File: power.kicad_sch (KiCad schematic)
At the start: 44 parts, among them IC302 L7805, IC303 L7805, J101 Test Points, P302 POWER, Q106 15 29, Q308 FR 32, Q503 BR 29, SW101 SW_SPDT

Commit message: General clean-up.
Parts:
- added TP2: ~, A-PCENGINE:Test_Point_1.5mm, symbol Connector:TestPoint
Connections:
- net +9V: now also TP2.1
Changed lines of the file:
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@@
   (junction (at 270.51 106.68) (diameter 0) (color 0 0 0 0)
+  )
+  (junction (at 253.365 36.83) (diameter 0) (color 0 0 0 0)
   )
   (junction (at 285.75 151.13) (diameter 0) (color 0 0 0 0)
@@
   )
   (wire (pts (xy 147.32 156.21) (xy 147.32 158.75))
+    (stroke (width 0) (type default))
+  )
+  (wire (pts (xy 253.365 36.83) (xy 256.286 36.83))
     (stroke (width 0) (type default))
   )
@@
         )
       )
+    )
+  )
+  (symbol (lib_id "Connector:TestPoint") (at 256.286 36.83 0) (unit 1)
+    (in_bom yes) (on_board yes) (dnp no)
+    (property "Reference" "TP2" (at 256.286 27.305 90)
+      (effects (font (size 1.27 1.27)) (justify right))
+    )
+    (property "Value" "~" (at 254.381 32.258 0)
+      (effects (font (size 1.27 1.27)) (justify right))
+    )
+    (property "Footprint" "A-PCENGINE:Test_Point_1.5mm" (at 261.366 36.83 0)
+      (effects (font (size 1.27 1.27)) hide)
+    )
+    (property "Datasheet" "~" (at 261.366 36.83 0)
+      (effects (font (size 1.27 1.27)) hide)
+    )
+    (pin "1")
+    (instances
+      (project "PCE"
+        (path "/c1c718c6-a427-431e-a18b-e46f94ae8e09/bb2f9872-1813-43e0-bcfc-5c5426bf43ce"
+          (reference "TP2") (unit 1)
+        )
+        (path "/c1c718c6-a427-431e-a18b-e46f94ae8e09/ba362b1f-3cb7-4861-9385-2b05dca17551"
+          (reference "TP70") (unit 1)
+        )
+      )

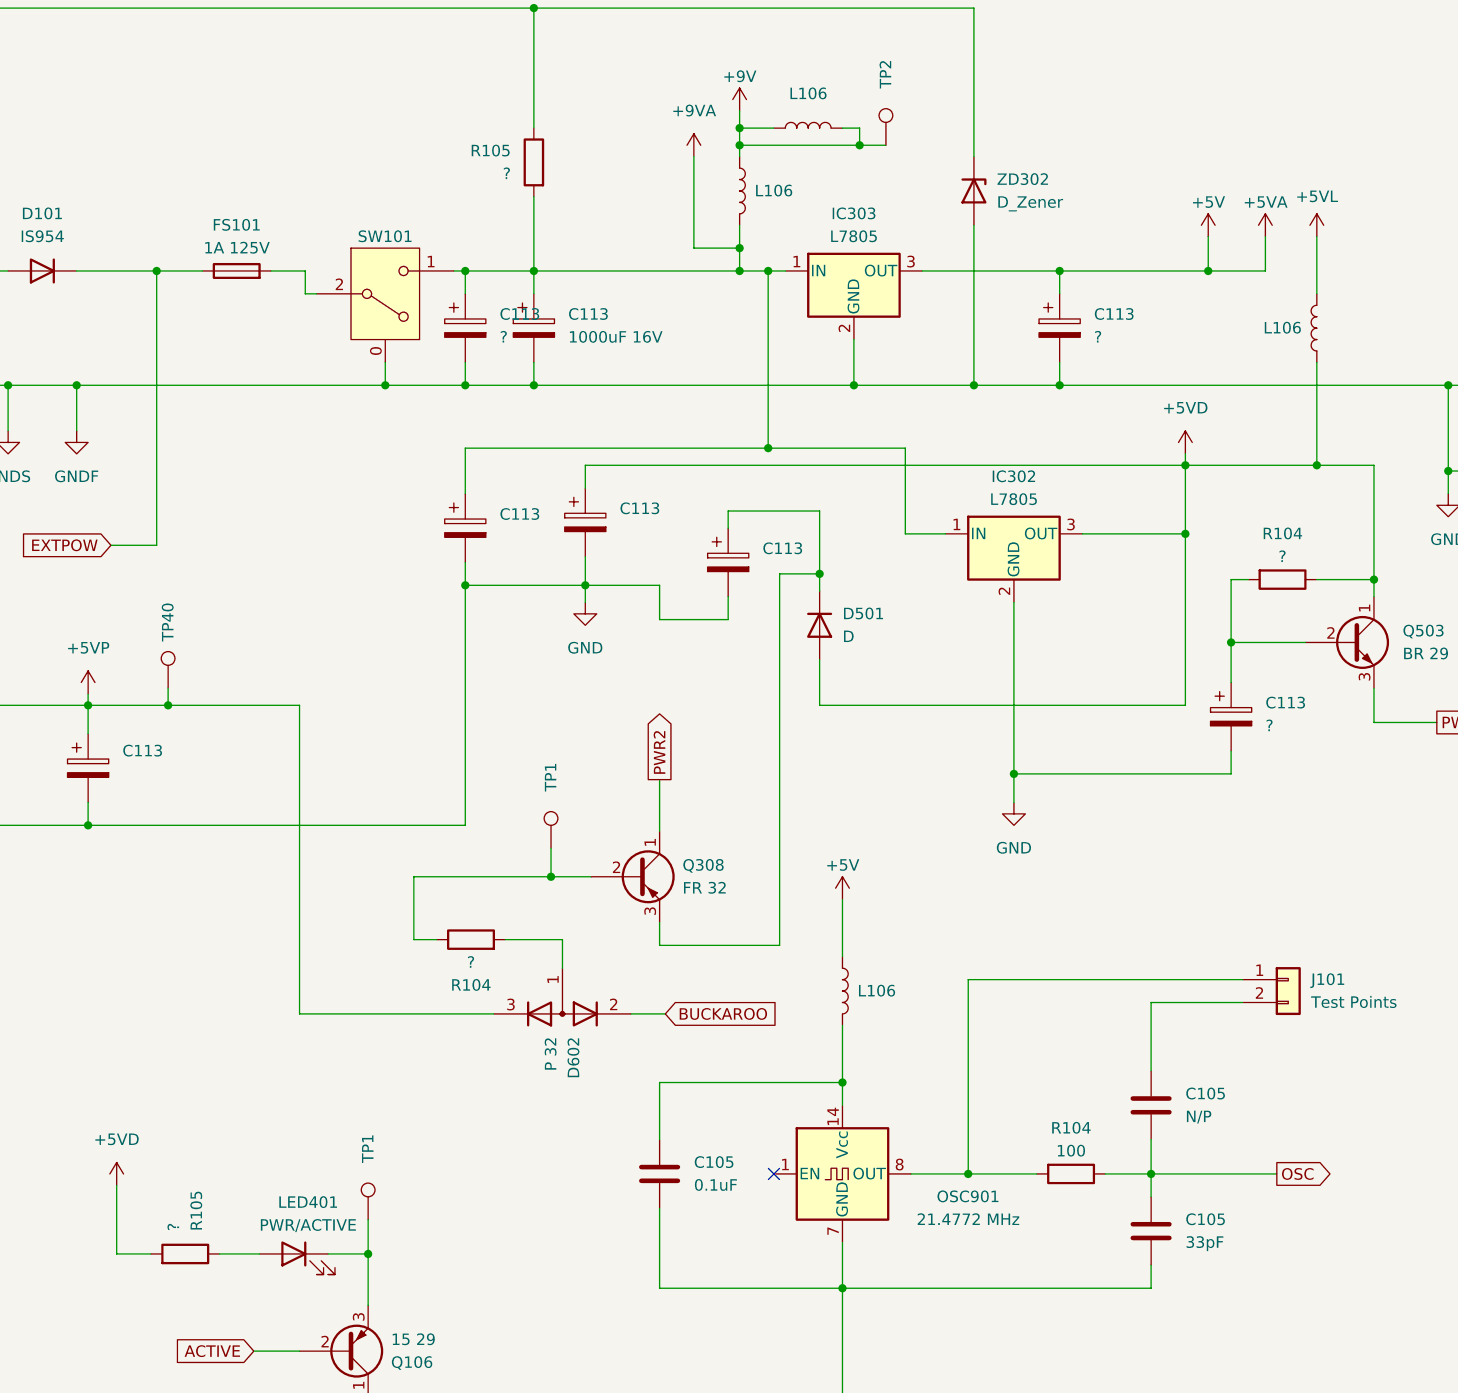
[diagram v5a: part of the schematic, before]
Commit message: Add resistor values to schematics.
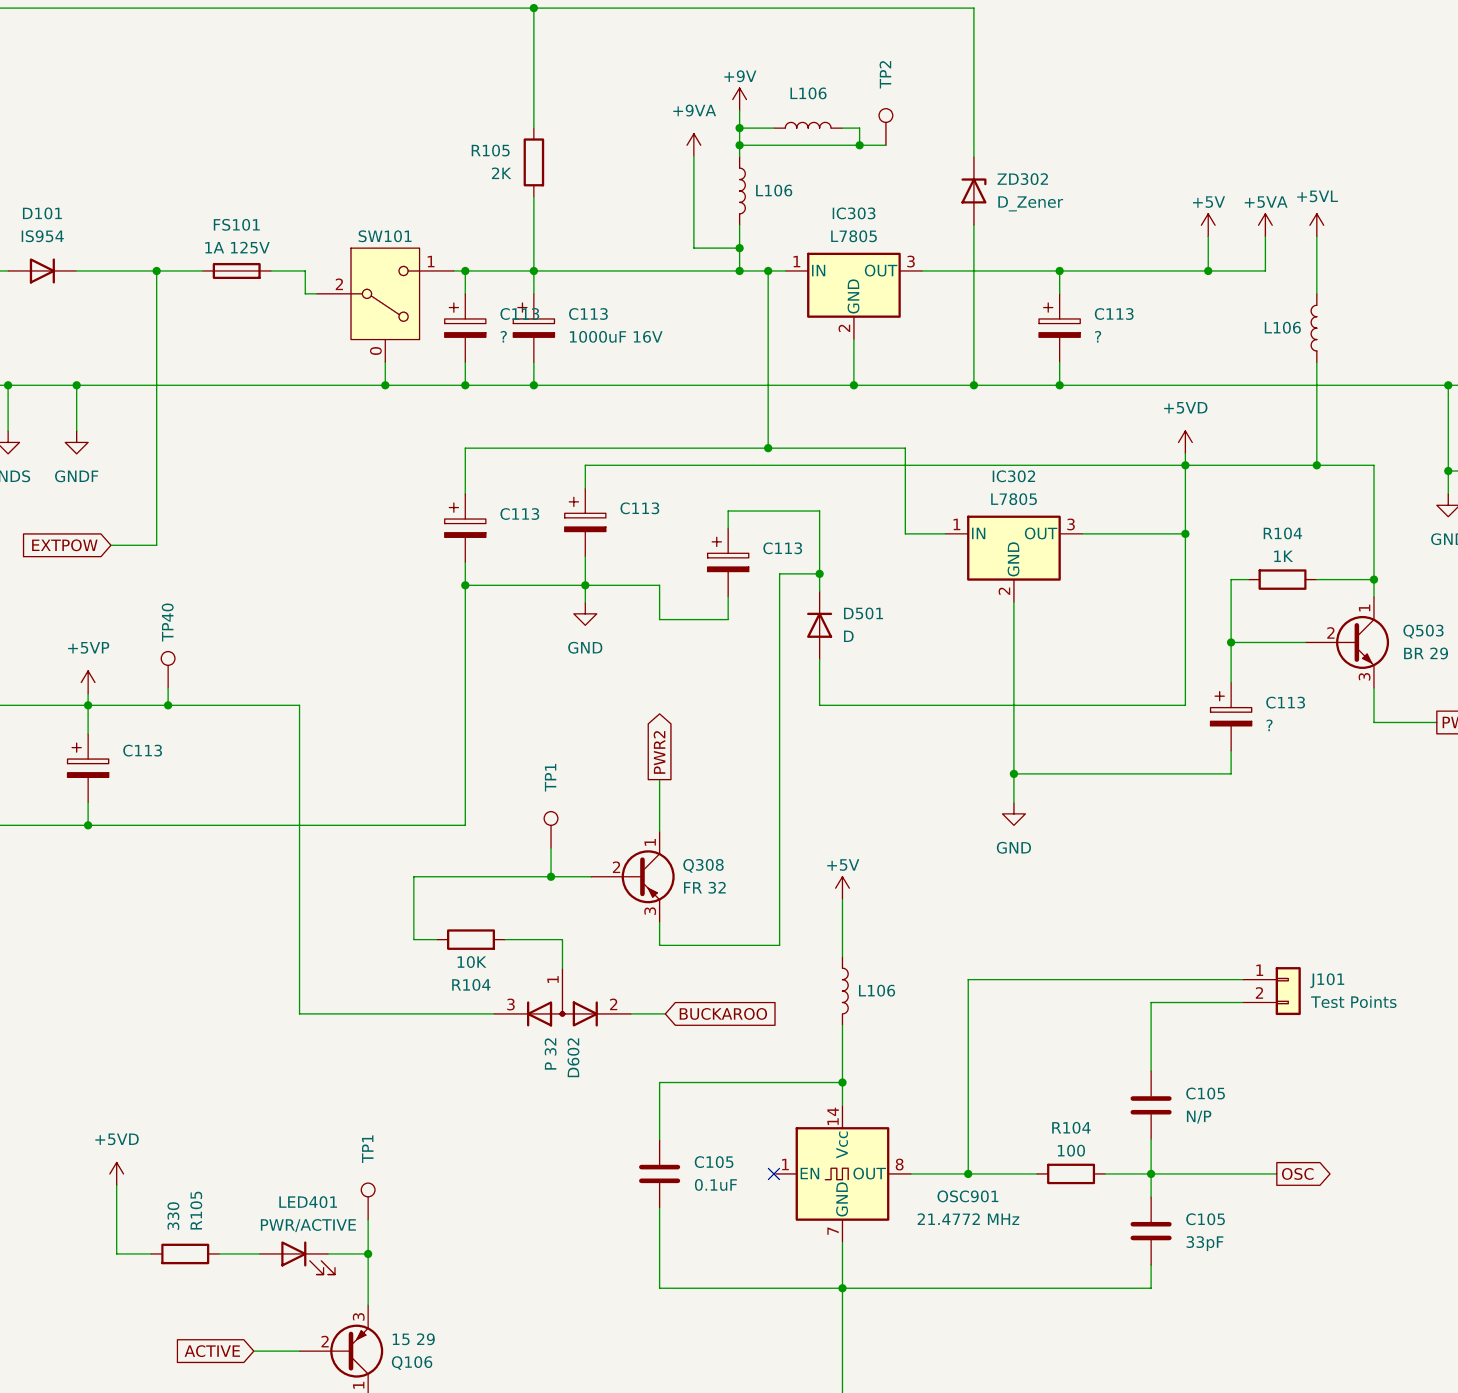
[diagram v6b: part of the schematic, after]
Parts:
- R104: value ? -> 1K
- R104: value ? -> 10K
- R105: value ? -> 330
- R105: value ? -> 2K
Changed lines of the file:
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@@
       (effects (font (size 1.27 1.27)) (justify left))
     )
-    (property "Value" "?" (at 177.165 157.48 0)
+    (property "Value" "330" (at 177.165 157.48 0)
       (effects (font (size 1.27 1.27)) (justify left))
     )
@@
       (effects (font (size 1.27 1.27)))
     )
-    (property "Value" "?" (at 300.355 82.55 90)
+    (property "Value" "1K" (at 300.355 82.55 90)
       (effects (font (size 1.27 1.27)))
     )
@@
       (effects (font (size 1.27 1.27)) (justify left))
     )
-    (property "Value" "?" (at 214.63 40.005 0)
+    (property "Value" "2K" (at 214.63 40.005 0)
       (effects (font (size 1.27 1.27)) (justify left))
     )
@@
       (effects (font (size 1.27 1.27)))
     )
-    (property "Value" "?" (at 210.185 127.635 90)
-      (effects (font (size 1.27 1.27)))
-    )
+    (property "Value" "10K" (at 210.185 127.635 90)
+      (effects (font (size 1.27 1.27)))
+    )

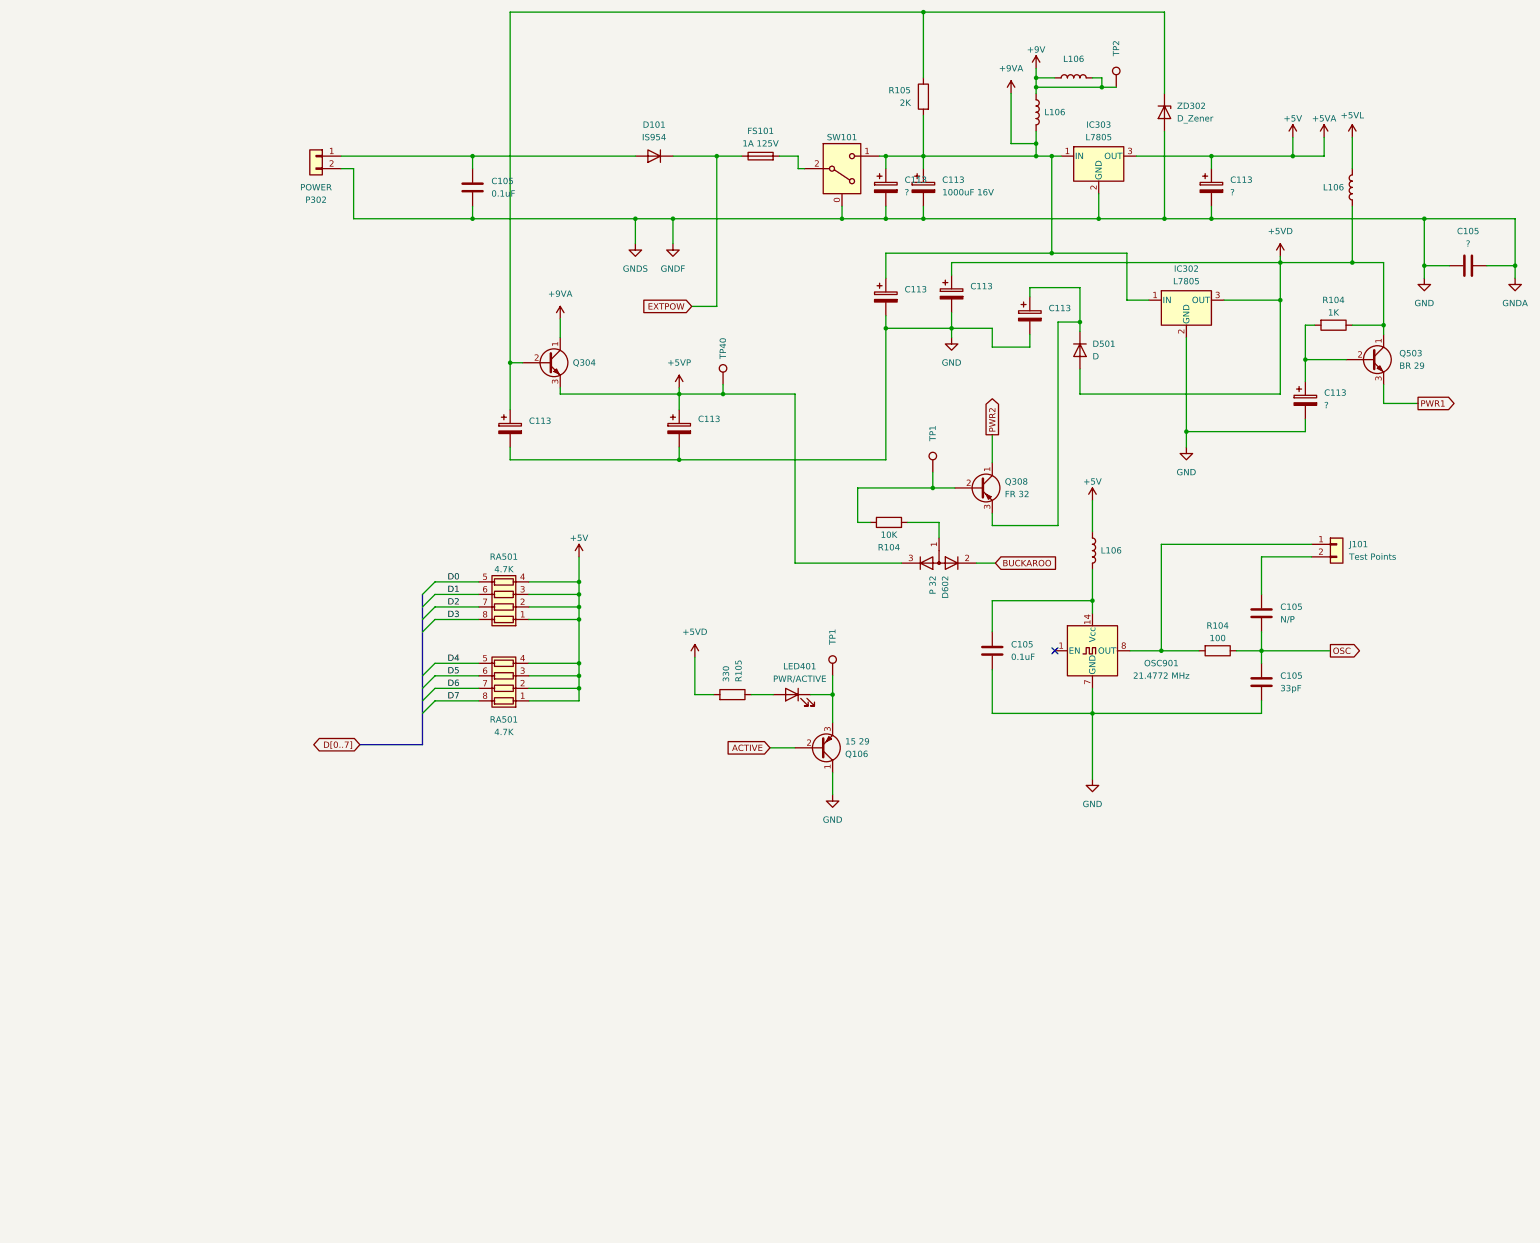
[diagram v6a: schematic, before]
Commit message: Schematic clean-up (IFU ASIC and other stuff).
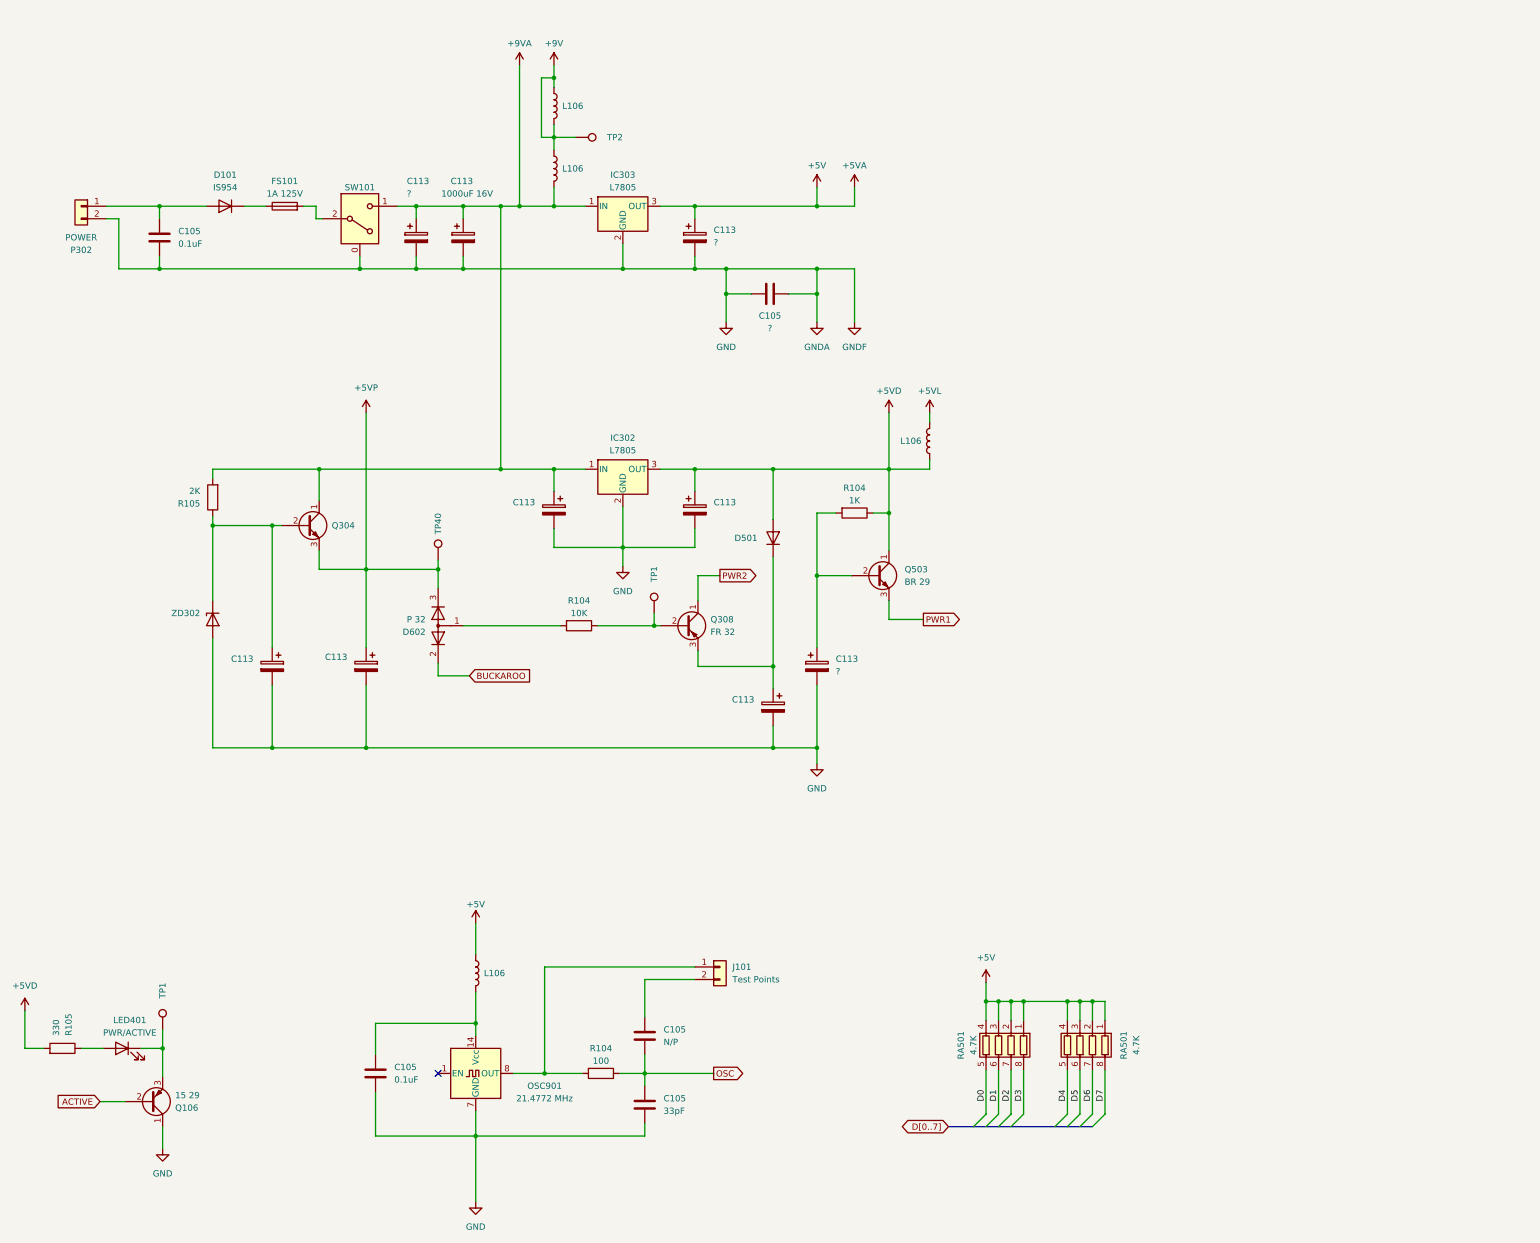
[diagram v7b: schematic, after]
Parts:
- D501: value D -> ~
- ZD302: value D_Zener -> ~
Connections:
- net EXTPOW: no longer names the net of D101.1 (K), FS101.1
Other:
- moved on the sheet: C105, C113, D101, D501, D602, FS101, IC302, IC303, J101, L106, LED401, OSC901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
